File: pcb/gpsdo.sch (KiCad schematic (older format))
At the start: 151 parts, among them IC1 ICE40LP384-SG32, J1 JTAG, J10 CLK0, J11 CLK7, J12 USB_B_Micro, J13 CLK6, J14 CLK5, J15 CLK4, J2 SSD1306, J3 EXT_CLOCK, J4 GPS_ANT, J5 USB_B_Micro, J6 CLK3, J7 Screw_Terminal_01x03, J8 CLK2, J9 CLK1, M1 E73-2G4M08S1C-52840, Q1 S9018, SW1 EC11, SW2 MCML4-112B, U1 MCP9808_MSOP, U2 MCP9808_MSOP, U3 TPS652510, U4 LT1763xS8, U5 74LVC1G17, U6 Si5351C-B-GM, U7 74LVC1G17, U8 uBlox NEO-7M, U9 AD5761R, Y1 32768, Y2 8663-XS

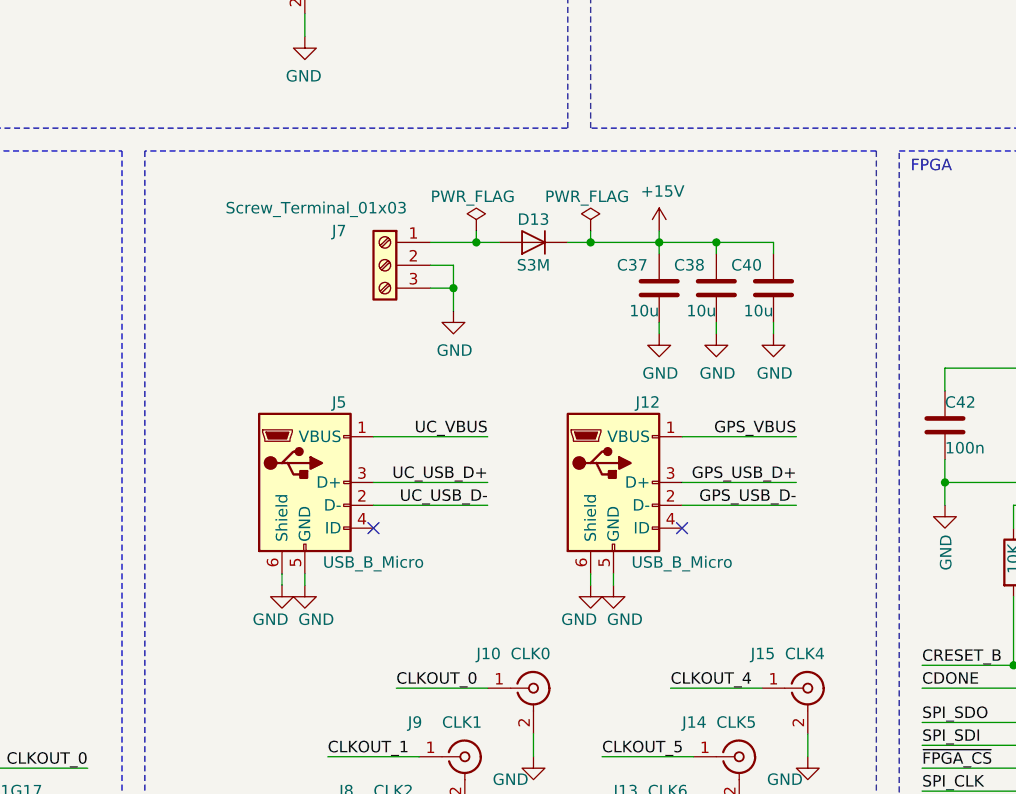
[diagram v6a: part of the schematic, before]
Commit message: add mounting holes, cleanup bord edge and mounting strategy. increase board size for that.
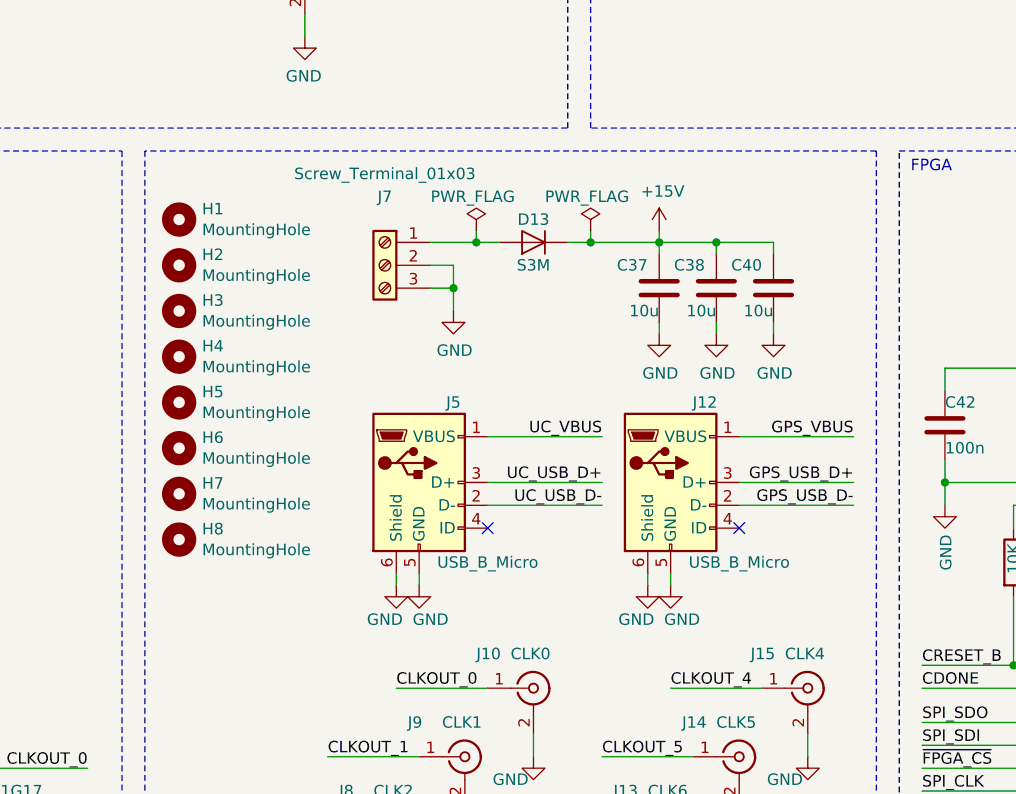
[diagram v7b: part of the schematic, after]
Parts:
- added H1, H2, H3, H4, H5, H6, H7, H8: MountingHole, MountingHole:MountingHole_4.3mm_M4_ISO14580_Pad, symbol Mechanical:MountingHole
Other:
- moved on the sheet: J12, J5
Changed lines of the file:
@@
 $EndComp
 Wire Wire Line
-	10900 6250 10400 6250
+	11400 6250 10900 6250
 Wire Wire Line
-	10400 6150 10900 6150
-NoConn ~ 10400 6350
-Text Label 10900 5950 2    50   ~ 0
+	10900 6150 11400 6150
+NoConn ~ 10900 6350
+Text Label 11400 5950 2    50   ~ 0
 UC_VBUS
 Wire Wire Line
-	10400 5950 10900 5950
+	10900 5950 11400 5950
 $Comp
 L Connector:USB_B_Micro J5
 U 1 1 5EF2FE6B
-P 10100 6150
-F 0 "J5" H 10250 6500 50  0000 C CNN
-F 1 "USB_B_Micro" H 10400 5800 50  0000 C CNN
-F 2 "dpiegdon:USB_Micro-B_Aliexpress_7.2mm_Pitch" H 10250 6100 50  0001 C CNN
-F 3 "~" H 10250 6100 50  0001 C CNN
-	1    10100 6150
+P 10600 6150
+F 0 "J5" H 10750 6500 50  0000 C CNN
+F 1 "USB_B_Micro" H 10900 5800 50  0000 C CNN
+F 2 "dpiegdon:USB_Micro-B_Aliexpress_7.2mm_Pitch" H 10750 6100 50  0001 C CNN
+F 3 "~" H 10750 6100 50  0001 C CNN
+	1    10600 6150
 	1    0    0    -1
 $EndComp
-Text Label 10900 6250 2    50   ~ 0
+Text Label 11400 6250 2    50   ~ 0
 UC_USB_D-
-Text Label 10900 6150 2    50   ~ 0
+Text Label 11400 6150 2    50   ~ 0
 UC_USB_D+
 $Comp
@@
 	1    0    0    -1
 $EndComp
-Text Label 12250 6250 2    50   ~ 0
+Text Label 12500 6250 2    50   ~ 0
 GPS_USB_D-
 $Comp
 L Connector:USB_B_Micro J12
 U 1 1 5EF6CFF3
-P 11450 6150
-F 0 "J12" H 11600 6500 50  0000 C CNN
-F 1 "USB_B_Micro" H 11750 5800 50  0000 C CNN
-F 2 "dpiegdon:USB_Micro-B_Aliexpress_7.2mm_Pitch" H 11600 6100 50  0001 C CNN
-F 3 "~" H 11600 6100 50  0001 C CNN
-	1    11450 6150
+P 11700 6150
+F 0 "J12" H 11850 6500 50  0000 C CNN
+F 1 "USB_B_Micro" H 12000 5800 50  0000 C CNN
+F 2 "dpiegdon:USB_Micro-B_Aliexpress_7.2mm_Pitch" H 11850 6100 50  0001 C CNN
+F 3 "~" H 11850 6100 50  0001 C CNN
+	1    11700 6150
 	1    0    0    -1
 $EndComp
 Wire Wire Line
-	11750 5950 12250 5950
-Text Label 12250 5950 2    50   ~ 0
+	12000 5950 12500 5950
+Text Label 12500 5950 2    50   ~ 0
 GPS_VBUS
-NoConn ~ 11750 6350
+NoConn ~ 12000 6350
 Wire Wire Line
-	11750 6150 12250 6150
+	12000 6150 12500 6150
 Wire Wire Line
-	11750 6250 12250 6250
-Text Label 12250 6150 2    50   ~ 0
+	12000 6250 12500 6250
+Text Label 12500 6150 2    50   ~ 0
 GPS_USB_D+
 Text Label 5100 10400 0    50   ~ 0
@@
 $EndComp
 Wire Wire Line
-	10100 6600 10100 6550
+	10600 6600 10600 6550
 Wire Wire Line
-	10000 6600 10000 6550
+	10500 6600 10500 6550
 $Comp
 L power:GND #PWR067
 U 1 1 60DD910B
-P 10000 6600
-F 0 "#PWR067" H 10000 6350 50  0001 C CNN
-F 1 "GND" H 9950 6450 50  0000 C CNN
-F 2 "" H 10000 6600 50  0001 C CNN
-F 3 "" H 10000 6600 50  0001 C CNN
-	1    10000 6600
+P 10500 6600
+F 0 "#PWR067" H 10500 6350 50  0001 C CNN
+F 1 "GND" H 10450 6450 50  0000 C CNN
+F 2 "" H 10500 6600 50  0001 C CNN
+F 3 "" H 10500 6600 50  0001 C CNN
+	1    10500 6600
 	1    0    0    -1
 $EndComp
@@
 L power:GND #PWR069
 U 1 1 5EF2FE79
-P 10100 6600
-F 0 "#PWR069" H 10100 6350 50  0001 C CNN
-F 1 "GND" H 10150 6450 50  0000 C CNN
-F 2 "" H 10100 6600 50  0001 C CNN
-F 3 "" H 10100 6600 50  0001 C CNN
-	1    10100 6600
+P 10600 6600
+F 0 "#PWR069" H 10600 6350 50  0001 C CNN
+F 1 "GND" H 10650 6450 50  0000 C CNN
+F 2 "" H 10600 6600 50  0001 C CNN
+F 3 "" H 10600 6600 50  0001 C CNN
+	1    10600 6600
 	1    0    0    -1
 $EndComp
 Wire Wire Line
-	11450 6600 11450 6550
+	11700 6600 11700 6550
 Wire Wire Line
-	11350 6600 11350 6550
+	11600 6600 11600 6550
 $Comp
 L power:GND #PWR076
 U 1 1 60E60959
-P 11350 6600
-F 0 "#PWR076" H 11350 6350 50  0001 C CNN
-F 1 "GND" H 11300 6450 50  0000 C CNN
-F 2 "" H 11350 6600 50  0001 C CNN
-F 3 "" H 11350 6600 50  0001 C CNN
-	1    11350 6600
+P 11600 6600
+F 0 "#PWR076" H 11600 6350 50  0001 C CNN
+F 1 "GND" H 11550 6450 50  0000 C CNN
+F 2 "" H 11600 6600 50  0001 C CNN
+F 3 "" H 11600 6600 50  0001 C CNN
+	1    11600 6600
 	1    0    0    -1
 $EndComp
@@
 L power:GND #PWR078
 U 1 1 60E60963
-P 11450 6600
-F 0 "#PWR078" H 11450 6350 50  0001 C CNN
-F 1 "GND" H 11500 6450 50  0000 C CNN
-F 2 "" H 11450 6600 50  0001 C CNN
-F 3 "" H 11450 6600 50  0001 C CNN
-	1    11450 6600
+P 11700 6600
+F 0 "#PWR078" H 11700 6350 50  0001 C CNN
+F 1 "GND" H 11750 6450 50  0000 C CNN
+F 2 "" H 11700 6600 50  0001 C CNN
+F 3 "" H 11700 6600 50  0001 C CNN
+	1    11700 6600
 	1    0    0    -1
 $EndComp
@@
 U 1 1 5E9A7252
 P 10450 5200
-F 0 "J7" H 10650 5350 50  0000 C CNN
-F 1 "Screw_Terminal_01x03" H 10750 5450 50  0000 C CNN
+F 0 "J7" H 10450 5500 50  0000 C CNN
+F 1 "Screw_Terminal_01x03" H 10450 5600 50  0000 C CNN
 F 2 "TerminalBlock_Phoenix:TerminalBlock_Phoenix_PT-1,5-3-5.0-H_1x03_P5.00mm_Horizontal" H 10450 5200 50  0001 C CNN
 F 3 "~" H 10450 5200 50  0001 C CNN
@@
 ENCODER_B
 NoConn ~ 13250 8100
+$Comp
+L Mechanical:MountingHole H1
+U 1 1 5EF7ACDA
+P 9550 5000
+F 0 "H1" H 9650 5046 50  0000 L CNN
+F 1 "MountingHole" H 9650 4955 50  0000 L CNN
+F 2 "MountingHole:MountingHole_4.3mm_M4_ISO14580_Pad" H 9550 5000 50  0001 C CNN
+F 3 "~" H 9550 5000 50  0001 C CNN
+	1    9550 5000
+	1    0    0    -1
+$EndComp
+$Comp
+L Mechanical:MountingHole H4
+U 1 1 5EF8906F
+P 9550 5600
+F 0 "H4" H 9650 5646 50  0000 L CNN
+F 1 "MountingHole" H 9650 5555 50  0000 L CNN
+F 2 "MountingHole:MountingHole_4.3mm_M4_ISO14580_Pad" H 9550 5600 50  0001 C CNN
+F 3 "~" H 9550 5600 50  0001 C CNN
+	1    9550 5600
+	1    0    0    -1
+$EndComp
+$Comp
+L Mechanical:MountingHole H3
+U 1 1 5EF88AF2
+P 9550 5400
+F 0 "H3" H 9650 5446 50  0000 L CNN
+F 1 "MountingHole" H 9650 5355 50  0000 L CNN
+F 2 "MountingHole:MountingHole_4.3mm_M4_ISO14580_Pad" H 9550 5400 50  0001 C CNN
+F 3 "~" H 9550 5400 50  0001 C CNN
+	1    9550 5400
+	1    0    0    -1
+$EndComp
+$Comp
+L Mechanical:MountingHole H2
+U 1 1 5EF885C1
+P 9550 5200
+F 0 "H2" H 9650 5246 50  0000 L CNN
+F 1 "MountingHole" H 9650 5155 50  0000 L CNN
+F 2 "MountingHole:MountingHole_4.3mm_M4_ISO14580_Pad" H 9550 5200 50  0001 C CNN
+F 3 "~" H 9550 5200 50  0001 C CNN
+	1    9550 5200
+	1    0    0    -1
+$EndComp
+$Comp
+L Mechanical:MountingHole H5
+U 1 1 5F2792E3
+P 9550 5800
+F 0 "H5" H 9650 5846 50  0000 L CNN
+F 1 "MountingHole" H 9650 5755 50  0000 L CNN
+F 2 "MountingHole:MountingHole_4.3mm_M4_ISO14580_Pad" H 9550 5800 50  0001 C CNN
+F 3 "~" H 9550 5800 50  0001 C CNN
+	1    9550 5800
+	1    0    0    -1
+$EndComp
+$Comp
+L Mechanical:MountingHole H8
+U 1 1 5F2792ED
+P 9550 6400
+F 0 "H8" H 9650 6446 50  0000 L CNN
+F 1 "MountingHole" H 9650 6355 50  0000 L CNN
+F 2 "MountingHole:MountingHole_4.3mm_M4_ISO14580_Pad" H 9550 6400 50  0001 C CNN
+F 3 "~" H 9550 6400 50  0001 C CNN
+	1    9550 6400
+	1    0    0    -1
+$EndComp
+$Comp
+L Mechanical:MountingHole H7
+U 1 1 5F2792F7
+P 9550 6200
+F 0 "H7" H 9650 6246 50  0000 L CNN
+F 1 "MountingHole" H 9650 6155 50  0000 L CNN
+F 2 "MountingHole:MountingHole_4.3mm_M4_ISO14580_Pad" H 9550 6200 50  0001 C CNN
+F 3 "~" H 9550 6200 50  0001 C CNN
+	1    9550 6200
+	1    0    0    -1
+$EndComp
+$Comp
+L Mechanical:MountingHole H6
+U 1 1 5F279301
+P 9550 6000
+F 0 "H6" H 9650 6046 50  0000 L CNN
+F 1 "MountingHole" H 9650 5955 50  0000 L CNN
+F 2 "MountingHole:MountingHole_4.3mm_M4_ISO14580_Pad" H 9550 6000 50  0001 C CNN
+F 3 "~" H 9550 6000 50  0001 C CNN
+	1    9550 6000
+	1    0    0    -1
+$EndComp
 $EndSCHEMATC

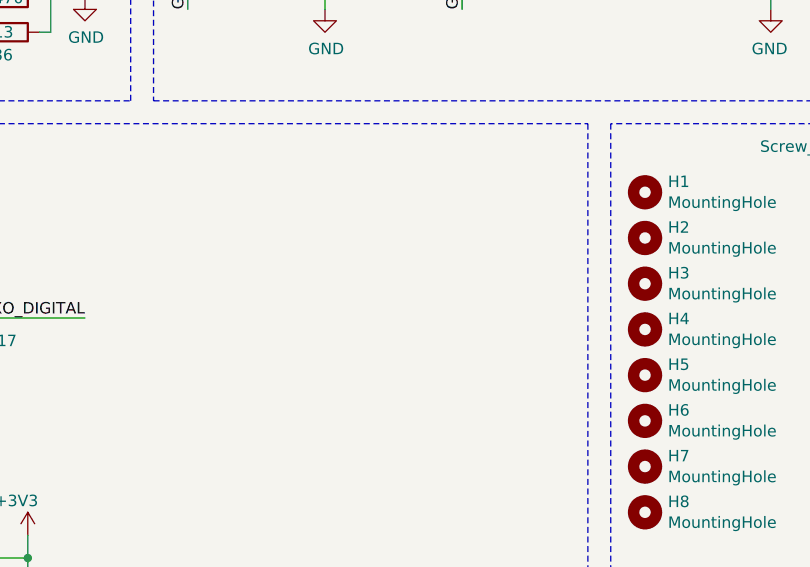
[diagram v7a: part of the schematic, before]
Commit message: added shield and more silkscreen, cleanup
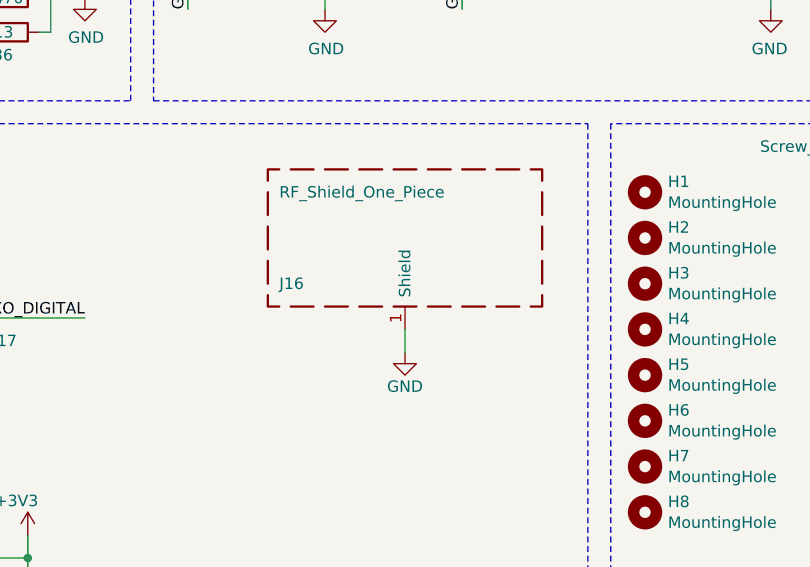
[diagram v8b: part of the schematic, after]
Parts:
- added J16: RF_Shield_One_Piece, RF_Shielding:Laird_Technologies_BMI-S-202-F_16.50x16.50mm, symbol Device:RF_Shield_One_Piece
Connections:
- net GND: now also J16.1 (Shield)
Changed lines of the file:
@@
+	1    0    0    -1
+$EndComp
+$Comp
+L Device:RF_Shield_One_Piece J16
+U 1 1 5EA2D598
+P 8500 5200
+F 0 "J16" H 7950 5000 50  0000 L CNN
+F 1 "RF_Shield_One_Piece" H 7950 5400 50  0000 L CNN
+F 2 "RF_Shielding:Laird_Technologies_BMI-S-202-F_16.50x16.50mm" H 8500 5100 50  0001 C CNN
+F 3 "~" H 8500 5100 50  0001 C CNN
+	1    8500 5200
+	1    0    0    -1
+$EndComp
+Wire Wire Line
+	8500 5600 8500 5700
+$Comp
+L power:GND #PWR0105
+U 1 1 5EB56E77
+P 8500 5700
+F 0 "#PWR0105" H 8500 5450 50  0001 C CNN
+F 1 "GND" H 8500 5550 50  0000 C CNN
+F 2 "" H 8500 5700 50  0001 C CNN
+F 3 "" H 8500 5700 50  0001 C CNN
+	1    8500 5700
 	1    0    0    -1
 $EndComp
